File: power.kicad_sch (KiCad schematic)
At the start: 26 parts, among them J1 Conn_01x03_Pin, J2 USB_C_Receptacle_PowerOnly_6P, U1 BQ24073RGTR, U2 TPS63802DLAR, U7 TPD1E10B06DPYR

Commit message: v1 Revision - Better routing - Added testpoints - DUCK - Tweaked drawings
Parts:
- added TP1, TP2, TP3: TestPoint, TestPoint:TestPoint_Pad_D1.0mm, symbol Connector:TestPoint
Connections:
- net +3V3: now also TP2.1
- net +BATT: now also TP3.1
- net VSYS: now also TP1.1
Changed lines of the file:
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@@
 	)
 	(junction
+		(at 121.92 114.3)
+		(diameter 0)
+		(color 0 0 0 0)
+	)
+	(junction
 		(at 40.64 146.05)
 		(diameter 0)
@@
 	(wire
 		(pts
-			(xy 127 114.3) (xy 116.84 114.3)
+			(xy 134.62 114.3) (xy 121.92 114.3)
 		)
 		(stroke
@@
 	(wire
 		(pts
-			(xy 127 110.49) (xy 127 114.3)
+			(xy 134.62 109.22) (xy 134.62 114.3)
 		)
 		(stroke
@@
 	(wire
 		(pts
+			(xy 121.92 114.3) (xy 116.84 114.3)
+		)
+		(stroke
+			(width 0)
+			(type default)
+		)
+	)
+	(wire
+		(pts
 			(xy 71.12 133.35) (xy 71.12 135.89)
 		)
@@
 	(symbol
 		(lib_id "power:+BATT")
-		(at 127 110.49 0)
+		(at 134.62 109.22 0)
 		(unit 1)
 		(exclude_from_sim no)
@@
 		(fields_autoplaced yes)
 		(property "Reference" "#PWR021"
-			(at 127 114.3 0)
+			(at 134.62 113.03 0)
 			(effects
 				(font
@@
 		)
 		(property "Value" "+BATT"
-			(at 127 105.41 0)
+			(at 134.62 104.14 0)
 			(effects
 				(font
@@
 		)
 		(property "Footprint" ""
-			(at 127 110.49 0)
+			(at 134.62 109.22 0)
 			(effects
 				(font
@@
 		)
 		(property "Datasheet" ""
-			(at 127 110.49 0)
+			(at 134.62 109.22 0)
 			(effects
 				(font
@@
 		)
 		(property "Description" "Power symbol creates a global label with name \"+BATT\""
-			(at 127 110.49 0)
+			(at 134.62 109.22 0)
 			(effects
 				(font
@@
 	)
 	(symbol
+		(lib_id "Connector:TestPoint")
+		(at 250.19 53.34 0)
+		(unit 1)
+		(exclude_from_sim no)
+		(in_bom no)
+		(on_board yes)
+		(dnp no)
+		(fields_autoplaced yes)
+		(property "Reference" "TP2"
+			(at 252.73 48.7679 0)
+			(effects
+				(font
+					(size 1.27 1.27)
+				)
+				(justify left)
+			)
+		)
+		(property "Value" "TestPoint"
+			(at 252.73 51.3079 0)
+			(effects
+				(font
+					(size 1.27 1.27)
+				)
+				(justify left)
+			)
+		)
+		(property "Footprint" "TestPoint:TestPoint_Pad_D1.0mm"
+			(at 255.27 53.34 0)
+			(effects
+				(font
+					(size 1.27 1.27)
+				)
+				(hide yes)
+			)
+		)
+		(property "Datasheet" "~"
+			(at 255.27 53.34 0)
+			(effects
+				(font
+					(size 1.27 1.27)
+				)
+				(hide yes)
+			)
+		)
+		(property "Description" "test point"
+			(at 250.19 53.34 0)
+			(effects
+				(font
+					(size 1.27 1.27)
+				)
+				(hide yes)
+			)
+		)
+		(pin "1"
+		)
+		(instances
+			(project "DRP.004"
+				(path "/990f0ec4-1b5b-4db8-8f39-ecd88fffeea0/6cce2e90-e51c-4942-a042-f4f9f078d271"
+					(reference "TP2")
+					(unit 1)
+				)
+			)
+		)
+	)
+	(symbol
 		(lib_id "power:GND")
 		(at 149.86 80.01 0)
@@
 	)
 	(symbol
+		(lib_id "Connector:TestPoint")
+		(at 121.92 114.3 0)
+		(unit 1)
+		(exclude_from_sim no)
+		(in_bom no)
+		(on_board yes)
+		(dnp no)
+		(fields_autoplaced yes)
+		(property "Reference" "TP3"
+			(at 124.46 109.7279 0)
+			(effects
+				(font
+					(size 1.27 1.27)
+				)
+				(justify left)
+			)
+		)
+		(property "Value" "TestPoint"
+			(at 124.46 112.2679 0)
+			(effects
+				(font
+					(size 1.27 1.27)
+				)
+				(justify left)
+			)
+		)
+		(property "Footprint" "TestPoint:TestPoint_Pad_D1.0mm"
+			(at 127 114.3 0)
+			(effects
+				(font
+					(size 1.27 1.27)
+				)
+				(hide yes)
+			)
+		)
+		(property "Datasheet" "~"
+			(at 127 114.3 0)
+			(effects
+				(font
+					(size 1.27 1.27)
+				)
+				(hide yes)
+			)
+		)
+		(property "Description" "test point"
+			(at 121.92 114.3 0)
+			(effects
+				(font
+					(size 1.27 1.27)
+				)
+				(hide yes)
+			)
+		)
+		(pin "1"
+		)
+		(instances
+			(project "DRP.004"
+				(path "/990f0ec4-1b5b-4db8-8f39-ecd88fffeea0/6cce2e90-e51c-4942-a042-f4f9f078d271"
+					(reference "TP3")
+					(unit 1)
+				)
+			)
+		)
+	)
+	(symbol
 		(lib_id "power:VBUS")
 		(at 48.26 35.56 0)
@@
 	)
 	(symbol
+		(lib_id "Connector:TestPoint")
+		(at 163.83 53.34 0)
+		(unit 1)
+		(exclude_from_sim no)
+		(in_bom no)
+		(on_board yes)
+		(dnp no)
+		(fields_autoplaced yes)
+		(property "Reference" "TP1"
+			(at 166.37 48.7679 0)
+			(effects
+				(font
+					(size 1.27 1.27)
+				)
+				(justify left)
+			)
+		)
+		(property "Value" "TestPoint"
+			(at 166.37 51.3079 0)
+			(effects
+				(font
+					(size 1.27 1.27)
+				)
+				(justify left)
+			)
+		)
+		(property "Footprint" "TestPoint:TestPoint_Pad_D1.0mm"
+			(at 168.91 53.34 0)
+			(effects
+				(font
+					(size 1.27 1.27)
+				)
+				(hide yes)
+			)
+		)
+		(property "Datasheet" "~"
+			(at 168.91 53.34 0)
+			(effects
+				(font
+					(size 1.27 1.27)
+				)
+				(hide yes)
+			)
+		)
+		(property "Description" "test point"
+			(at 163.83 53.34 0)
+			(effects
+				(font
+					(size 1.27 1.27)
+				)
+				(hide yes)
+			)
+		)
+		(pin "1"
+		)
+		(instances
+			(project ""
+				(path "/990f0ec4-1b5b-4db8-8f39-ecd88fffeea0/6cce2e90-e51c-4942-a042-f4f9f078d271"
+					(reference "TP1")
+					(unit 1)
+				)
+			)
+		)
+	)
+	(symbol
 		(lib_id "Device:L")
 		(at 207.01 34.29 90)
@@
 	)
 	(sheet
-		(at 183.515 112.395)
+		(at 212.725 111.125)
 		(size 56.515 34.29)
 		(exclude_from_sim no)
@@
 		)
 		(property "Sheetname" "power_control"
-			(at 183.515 111.6834 0)
+			(at 212.725 110.4134 0)
 			(effects
 				(font
@@
 		)
 		(property "Sheetfile" "power_control.kicad_sch"
-			(at 183.515 147.2696 0)
+			(at 212.725 145.9996 0)
 			(effects
 				(font

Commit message: Removed C5 Improved layout
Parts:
- removed C5: 22uF, Capacitor_SMD:C_0603_1608Metric, symbol Device:C
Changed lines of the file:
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@@
 	)
 	(junction
-		(at 273.05 66.04)
-		(diameter 0)
-		(color 0 0 0 0)
-	)
-	(junction
 		(at 59.69 35.56)
 		(diameter 0)
@@
 	)
 	(junction
-		(at 273.05 53.34)
-		(diameter 0)
-		(color 0 0 0 0)
-	)
-	(junction
 		(at 121.92 40.64)
 		(diameter 0)
@@
 	(wire
 		(pts
-			(xy 273.05 63.5) (xy 273.05 66.04)
-		)
-		(stroke
-			(width 0)
-			(type default)
-		)
-	)
-	(wire
-		(pts
 			(xy 72.39 120.65) (xy 72.39 121.92)
 		)
@@
 	(wire
 		(pts
-			(xy 273.05 55.88) (xy 273.05 53.34)
-		)
-		(stroke
-			(width 0)
-			(type default)
-		)
-	)
-	(wire
-		(pts
 			(xy 66.04 144.78) (xy 66.04 147.32)
 		)
@@
 					(unit 1)
 				)
-			)
-		)
-	)
-	(symbol
-		(lib_id "Device:C")
-		(at 273.05 59.69 0)
-		(mirror y)
-		(unit 1)
-		(exclude_from_sim no)
-		(in_bom yes)
-		(on_board yes)
-		(dnp yes)
-		(fields_autoplaced yes)
-		(property "Reference" "C5"
-			(at 276.86 58.4199 0)
-			(effects
-				(font
-					(size 1.27 1.27)
-				)
-				(justify right)
-			)
-		)
-		(property "Value" "22uF"
-			(at 276.86 60.9599 0)
-			(effects
-				(font
-					(size 1.27 1.27)
-				)
-				(justify right)
-			)
-		)
-		(property "Footprint" "Capacitor_SMD:C_0603_1608Metric"
-			(at 272.0848 63.5 0)
-			(effects
-				(font
-					(size 1.27 1.27)
-				)
-				(hide yes)
-			)
-		)
-		(property "Datasheet" "~"
-			(at 273.05 59.69 0)
-			(effects
-				(font
-					(size 1.27 1.27)
-				)
-				(hide yes)
-			)
-		)
-		(property "Description" "Unpolarized capacitor"
-			(at 273.05 59.69 0)
-			(effects
-				(font
-					(size 1.27 1.27)
-				)
-				(hide yes)
-			)
-		)
-		(property "lcsc" ""
-			(at 273.05 59.69 0)
-			(effects
-				(font
-					(size 1.27 1.27)
-				)
-			)
-		)
-		(pin "2"
-		)
-		(pin "1"
-		)
-		(instances
-			(project "DRP.004"
-				(path "/990f0ec4-1b5b-4db8-8f39-ecd88fffeea0/6cce2e90-e51c-4942-a042-f4f9f078d271"
-					(reference "C5")
-					(unit 1)
-				)

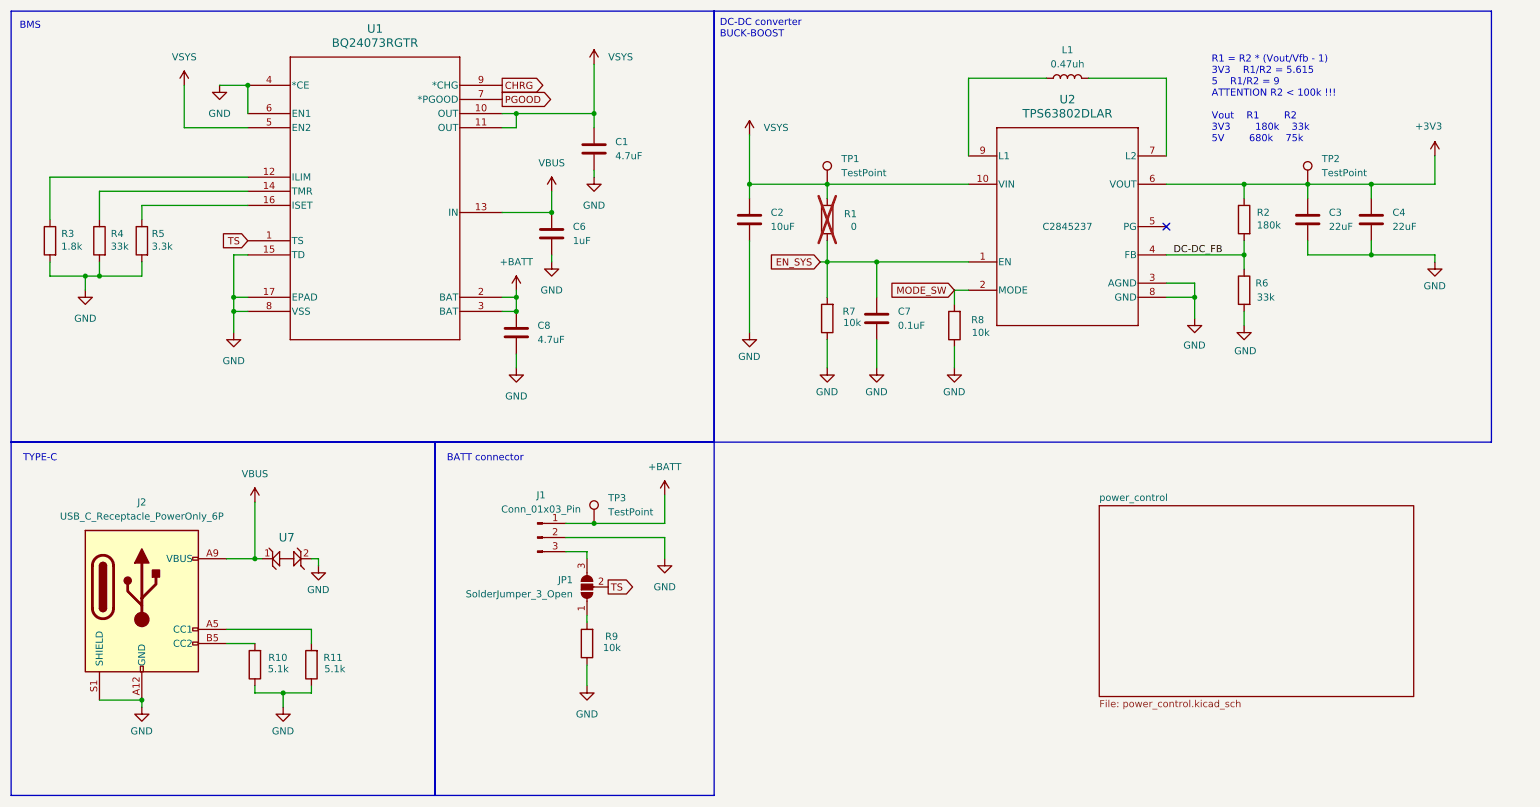
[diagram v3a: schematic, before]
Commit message: Rough placment of components for v3
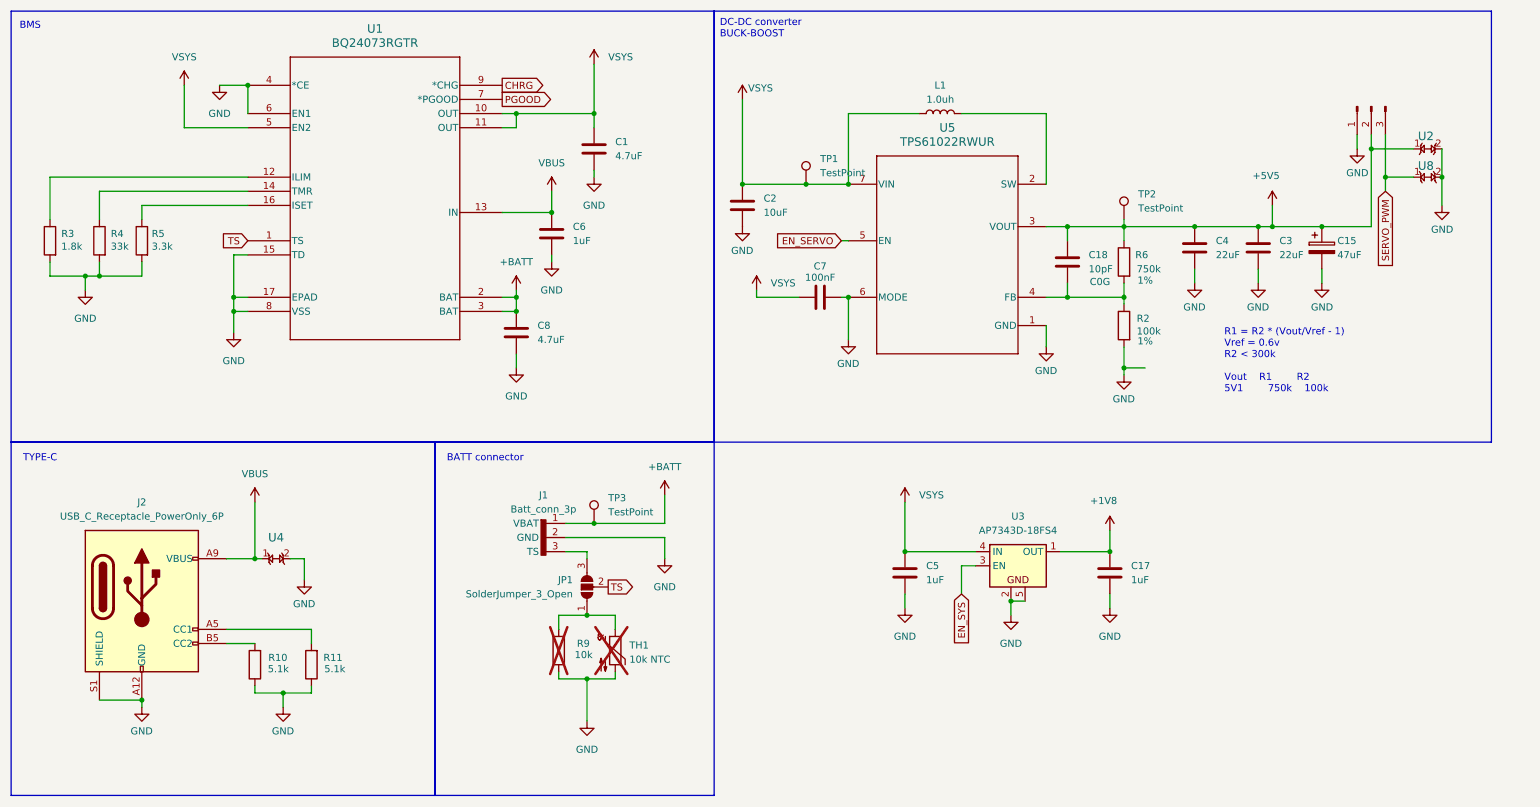
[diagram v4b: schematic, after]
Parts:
- removed J1: Conn_01x03_Pin, conn:JST_PH_S3B-PH-K_1x03_P2.00mm_Horizontal, symbol Connector:Conn_01x03_Pin
- removed R1: 0, Resistor_SMD:R_0603_1608Metric, symbol Device:R
- removed R7, R8: 10k, Resistor_SMD:R_0603_1608Metric, symbol Device:R
- removed U2: TPS63802DLAR, TPS63802:DLA0010A, symbol TPS63802:TPS63802DLAR
- removed U7: TPD1E10B06DPYR, TPD1E10B06DPYR:X1SON-2_L1.0-W0.6-P0.65-BI, symbol TPD1E10B06DPYR:TPD1E10B06DPYR
- added C15: 47uF, Capacitor_Tantalum_SMD:CP_EIA-3216-18_Kemet-A_HandSolder, symbol Device:C_Polarized
- added C17, C5: 1uF, Capacitor_SMD:C_0603_1608Metric, symbol Device:C
- added C18: 10pF, Capacitor_SMD:C_0402_1005Metric, symbol Device:C
- added J1: Batt_conn_3p, Muffin_CONNECTOR_THT:BATTERY_P2+P1.27mm_Horizontal, symbol Muffin_CONNECTORS:Batt_conn_3p
- added J3: Conn_01x03_Pin, conn:PinHeader_1x03_P2.54mm_Horizontal, symbol Connector:Conn_01x03_Pin
- added TH1: 10k NTC, Resistor_THT:R_Axial_DIN0204_L3.6mm_D1.6mm_P1.90mm_Vertical, symbol Device:Thermistor_NTC
- added U2, U4, U8: TPD1E10B06DPYR, Muffin_SMD:X1SON-2_L1.0-W0.6-P0.65-BI, symbol Muffin_DIODES:TPD1E10B06DPYR
- added U3: AP7343D-18FS4, Muffin_SMD:X2SON-4_1x1mm_P0.65mm, symbol Muffin_LDO:AP7343D-18FS4
- added U5: TPS61022RWUR, Muffin_SMD:RWU0007A, symbol Muffin_DC-DC:TPS61022RWUR
- C3, C4: footprint Capacitor_SMD:C_0603_1608Metric -> Capacitor_SMD:C_0805_2012Metric
- C7: value 0.1uF -> 100nF; footprint Capacitor_SMD:C_0603_1608Metric -> Capacitor_SMD:C_0402_1005Metric
- L1: value 0.47uh -> 1.0uh; footprint Inductor_SMD:L_0805_2012Metric_Pad1.05x1.20mm_HandSolder -> Inductor_SMD:L_1008_2520Metric
- R2: value 180k -> 100k; footprint Resistor_SMD:R_0603_1608Metric -> Resistor_SMD:R_0402_1005Metric; Tolerance  (none) -> 1%
- R6: value 33k -> 750k; footprint Resistor_SMD:R_0603_1608Metric -> Resistor_SMD:R_0402_1005Metric; Tolerance (none) -> 1%
- R9: now not fitted
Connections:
- net +BATT: now also J1.1 (VBAT)
- net EN_SYS: now also U3.3 (EN); no longer C7.1
- net GND: now also C7.1, R2.2, C15.2, C17.2, C5.2, J1.2 (GND), J3.1 (Pin_1), TH1.2, U2.2, U3.2, U3.5, U4.2, U5.1 (GND), U5.6 (MODE), U8.2; no longer C7.2, R6.2
- net VBUS: now also U4.1
- net VSYS: now also C7.2, L1.1, C5.1, U3.4 (IN), U5.7 (VIN)
- net at L1.2: now also U5.2 (SW)
- net at JP1.1 (A), R9.2: now also TH1.1
- net at JP1.3 (B): now also J1.3 (TS)
- net +3V3 renamed +5V5
- net +5V5: now also R6.1, C15.1, C18.1, J3.2 (Pin_2), U2.1, U5.3 (VOUT); no longer R2.1
- removed net DC-DC_FB: R2.2, R6.1
- new net: C18.2, R2.1, R6.2, U5.4 (FB)
- new net +1V8: C17.1, U3.1 (OUT)
- new net EN_SERVO: U5.5 (EN)
- new net SERVO_PWM: J3.3 (Pin_3), U8.1
- no-connect marks 1 -> 0
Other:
- removed sheet power_control
- note added: "R1 = R2 * (Vout/Vref - 1) Vref = 0.6v R2 < 300k Vout R1 R2 5V1 750k 100k"
- note removed: "R1 = R2 * (Vout/Vfb - 1) 3V3 R1/R2 = 5.615 5 R1/R2 = 9 ATTENTION R2 < 100k !!! Vout R1 R2 3V3 180k 33k 5V 680k 75k"
- moved on the sheet: C2, C3, C4, L1, R2, R6, TP1, TP2

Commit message: Routed v3
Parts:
- removed C15: 47uF, Capacitor_Tantalum_SMD:CP_EIA-3216-18_Kemet-A_HandSolder, symbol Device:C_Polarized
- removed TP1, TP2: TestPoint, TestPoint:TestPoint_Pad_D1.0mm, symbol Connector:TestPoint
- removed U3: AP7343D-18FS4, Muffin_SMD:X2SON-4_1x1mm_P0.65mm, symbol Muffin_LDO:AP7343D-18FS4
- added TP10: TestPoint, TestPoint:TestPoint_Pad_D1.0mm, symbol Connector:TestPoint
- added U7: AP2112K-1.8, Package_TO_SOT_SMD:SOT-23-5, symbol Regulator_Linear:AP2112K-1.8
- C2: footprint Capacitor_SMD:C_0603_1608Metric -> Capacitor_SMD:C_0805_2012Metric
- C7: value 100nF -> 0.1uF; footprint Capacitor_SMD:C_0402_1005Metric -> Capacitor_SMD:C_0603_1608Metric
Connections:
- net +1V8: now also TP10.1, U7.5 (VOUT)
- net EN_SYS: now also C7.2, U7.3 (EN)
- net GND: now also U7.2 (GND)
- net VSYS: now also U7.1 (VIN); no longer C7.2
- net BOOST_SW: now reaches L1.2, U5.2 (SW)
- net BOOST_FB: now reaches C18.2, R2.1, R6.2, U5.4 (FB)
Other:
- moved on the sheet: C17, C18, C3, C4, R2, R6

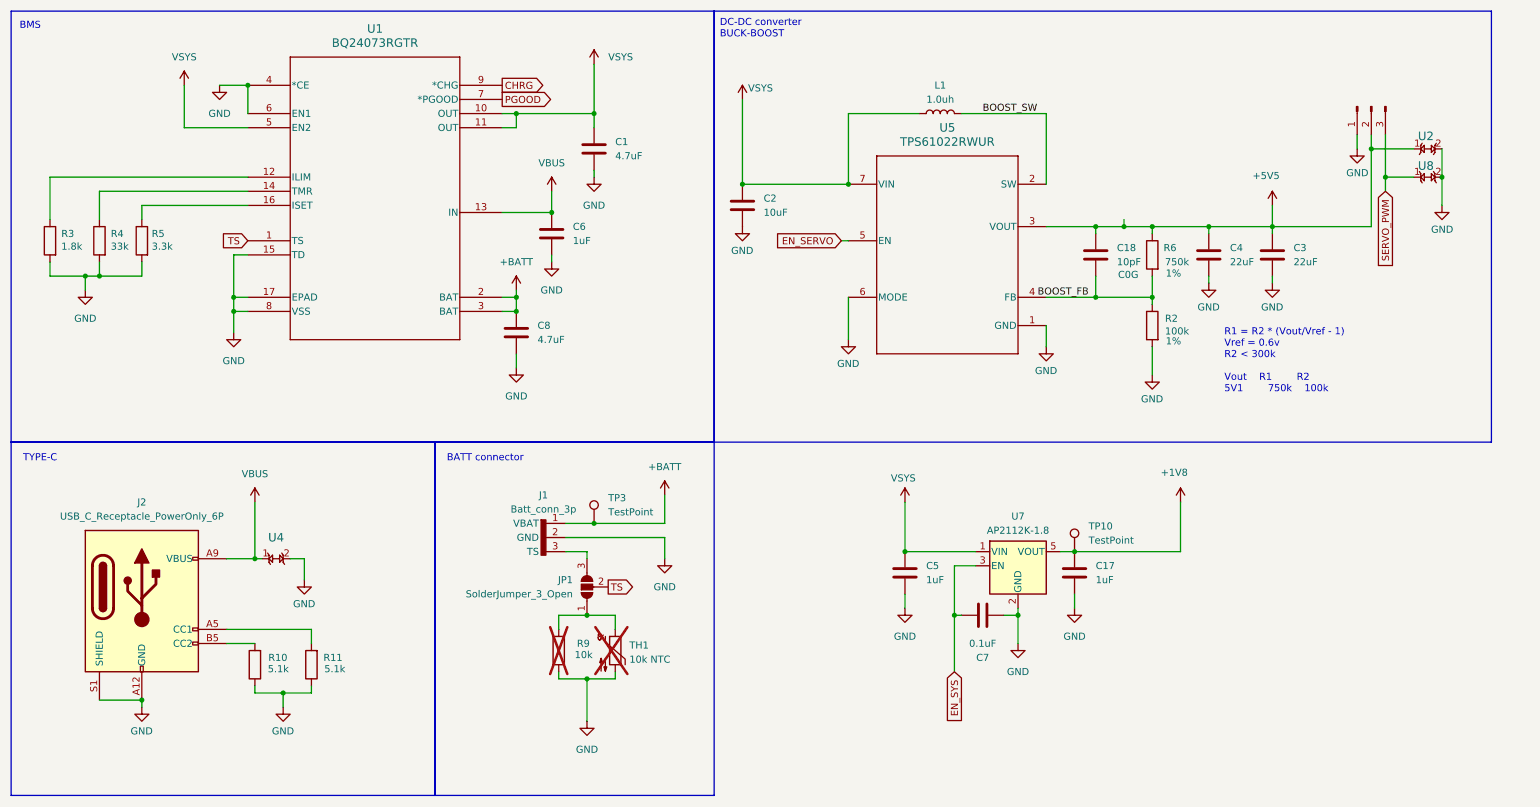
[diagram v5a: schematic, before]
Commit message: Moved servo logic to 5v
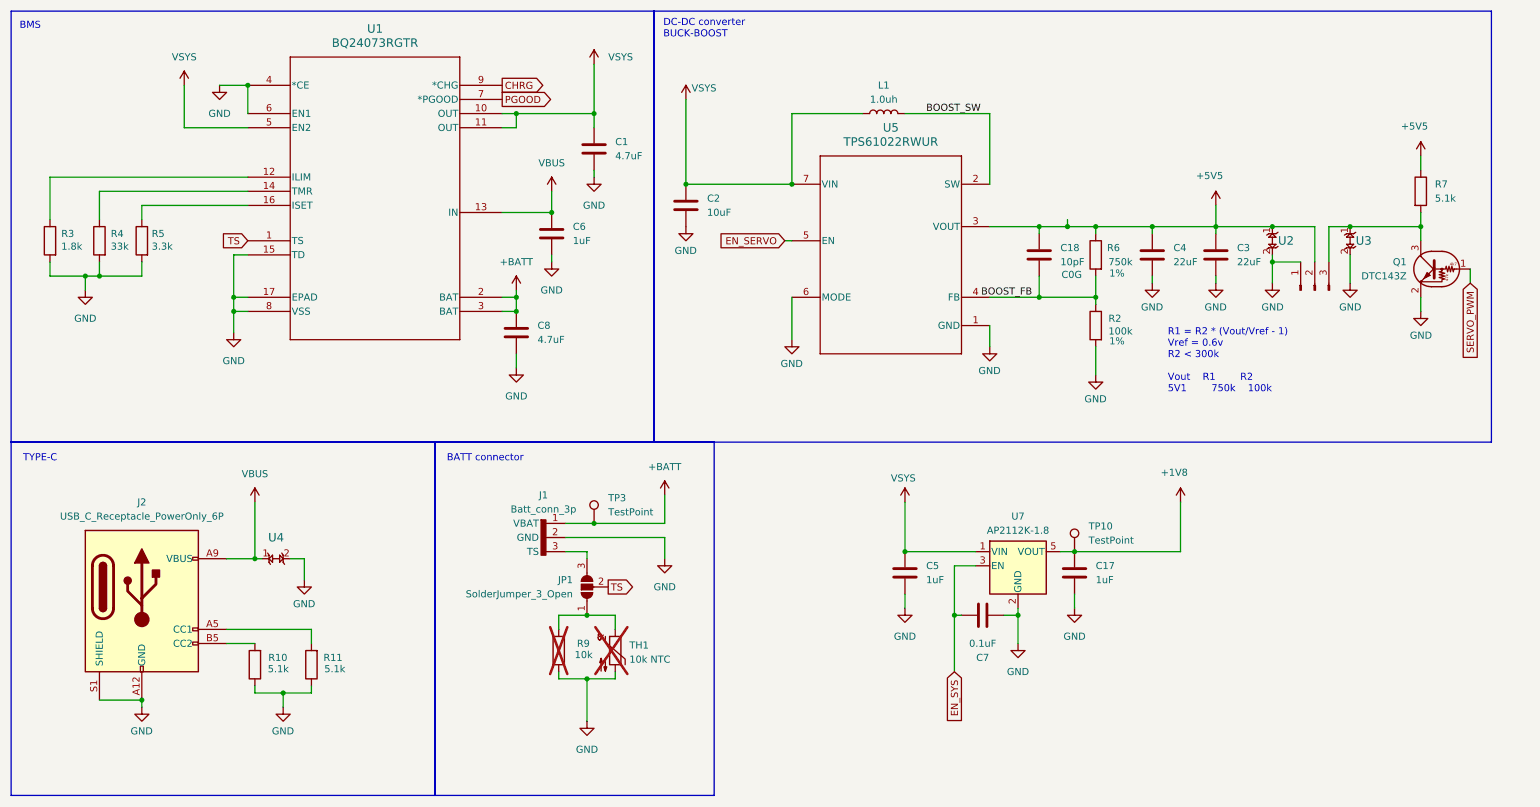
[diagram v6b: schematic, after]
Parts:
- removed U8: TPD1E10B06DPYR, Muffin_SMD:X1SON-2_L1.0-W0.6-P0.65-BI, symbol Muffin_DIODES:TPD1E10B06DPYR
- added Q1: DTC143Z, SOT-523:SOT-523, symbol Transistor_BJT:DTC143Z
- added R7: 5.1k, Resistor_SMD:R_0603_1608Metric, symbol Device:R
- added U3: TPD1E10B06DPYR, Muffin_SMD:X1SON-2_L1.0-W0.6-P0.65-BI, symbol Muffin_DIODES:TPD1E10B06DPYR
- J3: footprint conn:PinHeader_1x03_P2.54mm_Horizontal -> Muffin_CONNECTOR_THT:PinHeader_1x03_P2.54mm_Horizontal
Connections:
- net +5V5: now also R7.1
- net GND: now also Q1.2 (E), U3.2
- net SERVO_PWM: now also Q1.1 (B); no longer J3.3 (Pin_3)
- new net: J3.3 (Pin_3), Q1.3 (C), R7.2, U3.1
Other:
- moved on the sheet: C18, C2, C3, C4, L1, R2, R6, U5

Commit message: Expanded documentation
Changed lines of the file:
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@@
-	)
-	(junction
-		(at 207.01 60.96)
-		(diameter 0)
-		(color 0 0 0 0)
 	)
 	(junction
@@
 	(wire
 		(pts
-			(xy 207.01 59.69) (xy 207.01 60.96)
-		)
-		(stroke
-			(width 0)
-			(type default)
-		)
-	)
-	(wire
-		(pts
 			(xy 69.85 120.65) (xy 69.85 124.46)
 		)
@@
 	(wire
 		(pts
-			(xy 201.93 60.96) (xy 207.01 60.96)
+			(xy 201.93 60.96) (xy 212.09 60.96)
 		)
 		(stroke
@@
 		)
 		(stroke
-			(width 0)
-			(type default)
-		)
-	)
-	(wire
-		(pts
-			(xy 207.01 60.96) (xy 212.09 60.96)
-		)
-		(stroke
